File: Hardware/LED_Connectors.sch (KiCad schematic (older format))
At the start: 28 parts, among them J1 Conn_02x03_Odd_Even, J2 Conn_01x08, SW1 SW_Push

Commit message: Update components for assembly, generate gerbers
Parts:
- R3: Comments (none) -> 50V 10kΩ -55℃~+155℃ - ±5% - - - Thick Film Resistors 62.5mW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; LCSC (none) -> C60489
- SW1: footprint Button_Switch_SMD:SW_SPST_TL3305A -> Button_Switch_SMD:SW_Push_1P1T_NO_6x6mm_H9.5mm; Comments (none) -> Top Actuated 50mA @ 12VDC Round Button 160gf SPST SMD Tacti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; LCSC (none) -> C480275
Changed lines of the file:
@@
 F 0 "SW1" H 2860 7345 50  0000 C CNN
 F 1 "SW_Push" H 2860 7254 50  0000 C CNN
-F 2 "Button_Switch_SMD:SW_SPST_TL3305A" H 2860 7260 50  0001 C CNN
+F 2 "Button_Switch_SMD:SW_Push_1P1T_NO_6x6mm_H9.5mm" H 2860 7260 50  0001 C CNN
 F 3 "~" H 2860 7260 50  0001 C CNN
+F 4 "C480275" H 2860 7060 50  0001 C CNN "LCSC"
+F 5 "Top Actuated 50mA @ 12VDC Round Button 160gf SPST SMD Tactile Switches ROHS" H 2860 7060 50  0001 C CNN "Comments"
 	1    2860 7060
 	1    0    0    -1
@@
 Wire Wire Line
 	2050 4990 2350 4990
-$Comp
-L Device:R_US R16
-U 1 1 6186D969
-P 1900 4990
-F 0 "R16" V 1695 4990 50  0000 C CNN
-F 1 "100" V 1786 4990 50  0000 C CNN
-F 2 "Resistor_SMD:R_0402_1005Metric" V 1940 4980 50  0001 C CNN
-F 3 "~" H 1900 4990 50  0001 C CNN
-	1    1900 4990
-	0    1    1    0
-$EndComp
 Wire Wire Line
 	1750 4990 1400 4990
@@
 F 2 "Resistor_SMD:R_0402_1005Metric" V 3130 6510 50  0001 C CNN
 F 3 "~" H 3090 6520 50  0001 C CNN
+F 4 "C60489" V 3090 6520 50  0001 C CNN "LCSC"
+F 5 "50V 10kΩ -55℃~+155℃ - ±5% - - - Thick Film Resistors 62.5mW ±100ppm/℃ 0402 Chip Resistor - Surface Mount ROHS" V 3090 6520 50  0001 C CNN "Comments"
 	1    3090 6520
 	0    1    1    0
@@
 Text Notes 1790 6120 0    50   ~ 0
 Push button\nAlso at main connector for external option\n
+$Comp
+L Device:R_US R16
+U 1 1 6186D969
+P 1900 4990
+F 0 "R16" V 1695 4990 50  0000 C CNN
+F 1 "100" V 1786 4990 50  0000 C CNN
+F 2 "Resistor_SMD:R_0402_1005Metric" V 1940 4980 50  0001 C CNN
+F 3 "~" H 1900 4990 50  0001 C CNN
+	1    1900 4990
+	0    1    1    0
+$EndComp
 $EndSCHEMATC

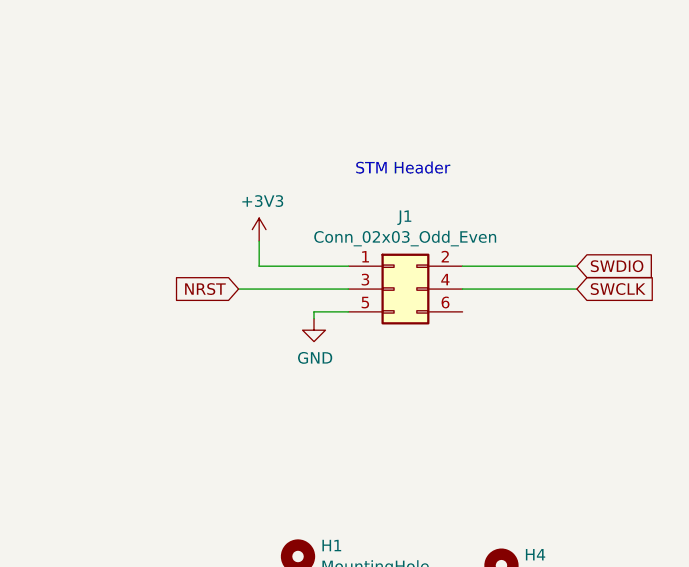
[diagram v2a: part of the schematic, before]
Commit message: Update board layout
Fix OLED pads to meet intended design. Move all non UI components to one side of the board for better single sided assembly.
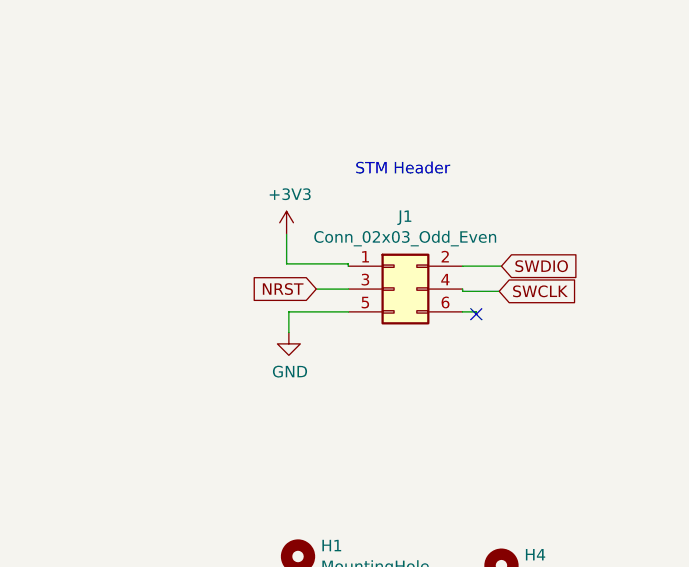
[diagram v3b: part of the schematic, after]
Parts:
- J1: footprint Connector_PinHeader_2.54mm:PinHeader_2x03_P2.54mm_Vertical_SMD -> Connector:Tag-Connect_TC2030-IDC-NL_2x03_P1.27mm_Vertical
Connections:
- no-connect marks 0 -> 1
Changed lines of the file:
@@
 L power:+3V3 #PWR0121
 U 1 1 613E42EE
-P 8480 4310
-F 0 "#PWR0121" H 8480 4160 50  0001 C CNN
-F 1 "+3V3" H 8495 4483 50  0000 C CNN
-F 2 "" H 8480 4310 50  0001 C CNN
-F 3 "" H 8480 4310 50  0001 C CNN
-	1    8480 4310
-	1    0    0    -1
-$EndComp
-Wire Wire Line
-	8390 4520 8870 4520
-Wire Wire Line
-	9370 4520 9870 4520
-Wire Wire Line
-	9370 4420 9870 4420
-Wire Wire Line
-	8480 4310 8480 4420
+P 8600 4280
+F 0 "#PWR0121" H 8600 4130 50  0001 C CNN
+F 1 "+3V3" H 8615 4453 50  0000 C CNN
+F 2 "" H 8600 4280 50  0001 C CNN
+F 3 "" H 8600 4280 50  0001 C CNN
+	1    8600 4280
+	1    0    0    -1
+$EndComp
 Wire Wire Line
 	9030 3070 9420 3070
@@
 Wire Wire Line
 	9420 2570 8980 2570
-Wire Wire Line
-	8480 4420 8870 4420
 $Comp
 L Mechanical:MountingHole H1
@@
 $EndComp
 $Comp
-L Connector_Generic:Conn_02x03_Odd_Even J1
-U 1 1 61BC1314
-P 9070 4520
-F 0 "J1" H 9120 4837 50  0000 C CNN
-F 1 "Conn_02x03_Odd_Even" H 9120 4746 50  0000 C CNN
-F 2 "Connector_PinHeader_2.54mm:PinHeader_2x03_P2.54mm_Vertical_SMD" H 9070 4520 50  0001 C CNN
-F 3 "~" H 9070 4520 50  0001 C CNN
-	1    9070 4520
-	1    0    0    -1
-$EndComp
-$Comp
 L Mechanical:MountingHole H4
 U 1 1 61F3BE63
@@
 L power:GND #PWR0163
 U 1 1 61889F2B
-P 8720 4650
-F 0 "#PWR0163" H 8720 4400 50  0001 C CNN
-F 1 "GND" H 8725 4477 50  0000 C CNN
-F 2 "" H 8720 4650 50  0001 C CNN
-F 3 "" H 8720 4650 50  0001 C CNN
-	1    8720 4650
-	1    0    0    -1
-$EndComp
-Wire Wire Line
-	8870 4620 8720 4620
-Wire Wire Line
-	8720 4620 8720 4650
+P 8610 4710
+F 0 "#PWR0163" H 8610 4460 50  0001 C CNN
+F 1 "GND" H 8615 4537 50  0000 C CNN
+F 2 "" H 8610 4710 50  0001 C CNN
+F 3 "" H 8610 4710 50  0001 C CNN
+	1    8610 4710
+	1    0    0    -1
+$EndComp
 Wire Wire Line
 	2650 4990 2800 4990
@@
 	1    0    0    -1
 $EndComp
-Text GLabel 9870 4420 2    50   Input ~ 0
+Text GLabel 9540 4420 2    50   Input ~ 0
 SWDIO
-Text GLabel 9870 4520 2    50   Input ~ 0
+Text GLabel 9530 4530 2    50   Input ~ 0
 SWCLK
-Text GLabel 8390 4520 0    50   Input ~ 0
+Text GLabel 8730 4520 0    50   Input ~ 0
 NRST
 Wire Wire Line
@@
 	0    1    1    0
 $EndComp
+Wire Wire Line
+	8600 4410 8870 4410
+Wire Wire Line
+	8870 4410 8870 4420
+Wire Wire Line
+	8600 4280 8600 4410
+Wire Wire Line
+	8730 4520 8870 4520
+Wire Wire Line
+	8610 4710 8610 4620
+Wire Wire Line
+	8610 4620 8870 4620
+Wire Wire Line
+	9370 4420 9540 4420
+Wire Wire Line
+	9530 4530 9370 4530
+Wire Wire Line
+	9370 4530 9370 4520
+NoConn ~ 9430 4630
+Wire Wire Line
+	9430 4630 9430 4620
+Wire Wire Line
+	9430 4620 9370 4620
+$Comp
+L Connector_Generic:Conn_02x03_Odd_Even J1
+U 1 1 61BC1314
+P 9070 4520
+F 0 "J1" H 9120 4837 50  0000 C CNN
+F 1 "Conn_02x03_Odd_Even" H 9120 4746 50  0000 C CNN
+F 2 "Connector:Tag-Connect_TC2030-IDC-NL_2x03_P1.27mm_Vertical" H 9070 4520 50  0001 C CNN
+F 3 "~" H 9070 4520 50  0001 C CNN
+	1    9070 4520
+	1    0    0    -1
+$EndComp
 $EndSCHEMATC

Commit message: Updates
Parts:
- R16: value 100 -> 1k
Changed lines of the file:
@@
 Title "CAN Gauge"
 Date "2021-10-10"
-Rev "B"
+Rev "C"
 Comp ""
 Comment1 ""
@@
 P 1900 4990
 F 0 "R16" V 1695 4990 50  0000 C CNN
-F 1 "100" V 1786 4990 50  0000 C CNN
+F 1 "1k" V 1786 4990 50  0000 C CNN
 F 2 "Resistor_SMD:R_0402_1005Metric" V 1940 4980 50  0001 C CNN
 F 3 "~" H 1900 4990 50  0001 C CNN
